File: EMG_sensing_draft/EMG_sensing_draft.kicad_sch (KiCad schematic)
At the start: 16 parts

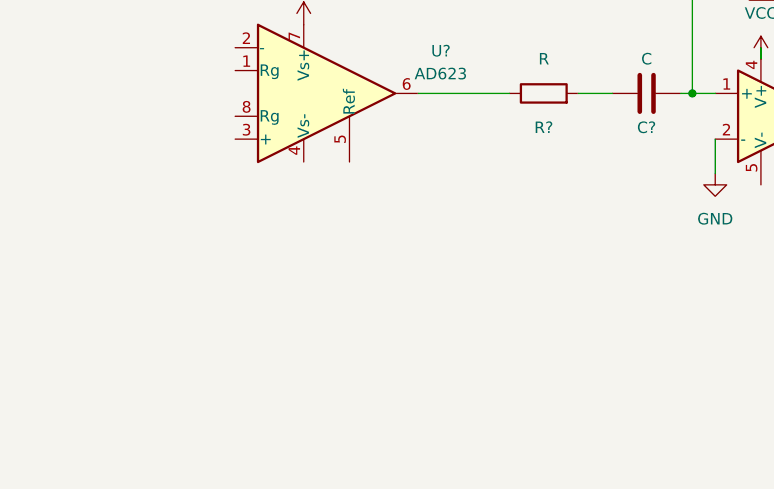
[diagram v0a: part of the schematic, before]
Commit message: Add parts folder and components
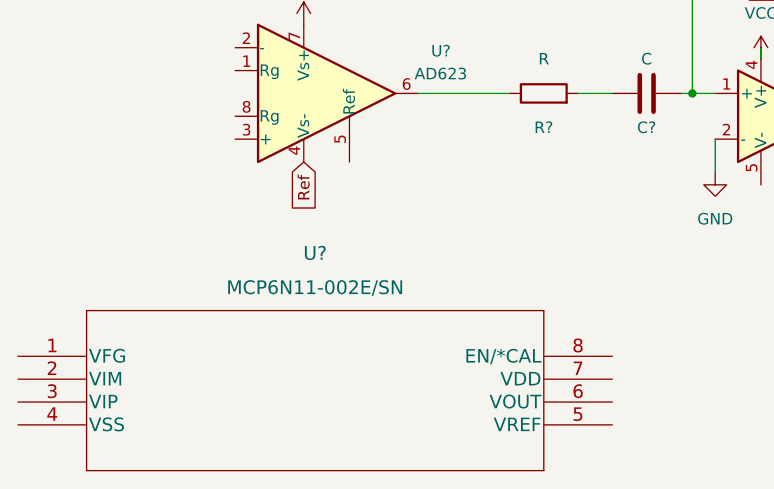
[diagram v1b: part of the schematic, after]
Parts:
- added U?: MCP6N11-002E/SN, SOIC8-N_MC_MCH, symbol MCP6N11:MCP6N11-002E/SN
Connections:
- net Ref: now reaches U?.4 (Vs-)
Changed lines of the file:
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@@
     (stroke (width 0) (type default) (color 0 0 0 0))
+  )
+  (global_label "Ref" (shape input) (at 66.04 109.22 270) (fields_autoplaced)
+    (effects (font (size 1.27 1.27)) (justify right))
+    (property "Intersheet References" "${INTERSHEET_REFS}" (id 0) (at 66.1194 114.7174 90)
+      (effects (font (size 1.27 1.27)) (justify right) hide)
+    )
   )
   (symbol (lib_id "Device:C") (at 229.87 85.09 90) (unit 1)
@@
     (pin "2")
   )
+  (symbol (lib_id "MCP6N11:MCP6N11-002E{slash}SN") (at 34.29 130.81 0) (unit 1)
+    (in_bom yes) (on_board yes) (fields_autoplaced)
+    (property "Reference" "U?" (id 0) (at 67.31 119.38 0)
+      (effects (font (size 1.524 1.524)))
+    )
+    (property "Value" "MCP6N11-002E/SN" (id 1) (at 67.31 123.19 0)
+      (effects (font (size 1.524 1.524)))
+    )
+    (property "Footprint" "SOIC8-N_MC_MCH" (id 2) (at 67.31 124.714 0)
+      (effects (font (size 1.524 1.524)) hide)
+    )
+    (property "Datasheet" "" (id 3) (at 34.29 130.81 0)
+      (effects (font (size 1.524 1.524)))
+    )
+    (pin "1")
+    (pin "2")
+    (pin "3")
+    (pin "4")
+    (pin "5")
+    (pin "6")
+    (pin "7")
+    (pin "8")
+  )
   (symbol (lib_id "Device:R") (at 156.21 90.17 90) (unit 1)
     (in_bom yes) (on_board yes)
@@
       (reference "R?") (unit 1) (value "R") (footprint "")
     )
+    (path "/4d7dc583-653d-4195-93a0-299e440aba51"
+      (reference "U?") (unit 1) (value "MCP6N11-002E/SN") (footprint "SOIC8-N_MC_MCH")
+    )
     (path "/6050b63c-7b0b-43e0-927f-cccf7bc57ee0"

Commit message: added Eclectronics folder
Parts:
- added J?: USB_A_0480370001, symbol Eclectronics:USB_A_0480370001
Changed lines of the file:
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@@
     (pin "1")
+  )
+  (symbol (lib_id "Eclectronics:USB_A_0480370001") (at 36.83 73.66 0) (unit 1)
+    (in_bom yes) (on_board yes) (fields_autoplaced)
+    (property "Reference" "J?" (id 0) (at 36.83 54.61 0)
+      (effects (font (size 1.524 1.524)))
+    )
+    (property "Value" "USB_A_0480370001" (id 1) (at 36.83 58.42 0)
+      (effects (font (size 1.524 1.524)))
+    )
+    (property "Footprint" "" (id 2) (at 45.72 69.85 0)
+      (effects (font (size 1.27 1.27)) hide)
+    )
+    (property "Datasheet" "" (id 3) (at 45.72 69.85 0)
+      (effects (font (size 1.27 1.27)) hide)
+    )
+    (pin "1")
+    (pin "2")
+    (pin "3")
+    (pin "4")
+    (pin "5")
+    (pin "6")
   )
   (symbol (lib_id "power:GND") (at 111.76 110.49 0) (unit 1)
@@
       (reference "D?") (unit 1) (value "DIODE") (footprint "")
     )
+    (path "/62cb1867-8881-4d82-894a-982d3e0ef0cf"
+      (reference "J?") (unit 1) (value "USB_A_0480370001") (footprint "")
+    )
     (path "/46275dcf-c1cf-4eed-86f4-1f3b88e55538"

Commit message: added inamp
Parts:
- removed U?: MCP6N11-002E/SN, SOIC8-N_MC_MCH, symbol MCP6N11:MCP6N11-002E/SN
- removed U?: AD623, symbol Amplifier_Instrumentation:AD623
- added J?: Conn_01x03, symbol Connector_Generic:Conn_01x03
- added R? (x2): R, symbol Device:R
- added U?: MCP6N11-002E/SN, SOIC8-N_MC_MCH, symbol MCP6N11:MCP6N11-002E/SN
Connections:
- net GND: now also U?.4 (VSS)
- net V_SIGNAL: now reaches C?.2, R?.2, U?.3
- net 5V: now reaches J?.1 (VBUS)
- net 5V: now also U?.7 (VDD)
- new net: R?.1, R?.2, U?.1 (VFG)
- new net VOUT: R?.2, U?.6 (VOUT)
- new net emg_node_one: J?.2 (Pin_2)
- new net emg_node_two: J?.1 (Pin_1)
- new net emg_ref: J?.3 (Pin_3), R?.1, U?.5 (VREF)
- new net emg_sensor_one: U?.2 (VIM)
- new net emg_sensor_two: U?.3 (VIP)
- no-connect marks 0 -> 3
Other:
- moved on the sheet: C?, D?, J?, R?, U?

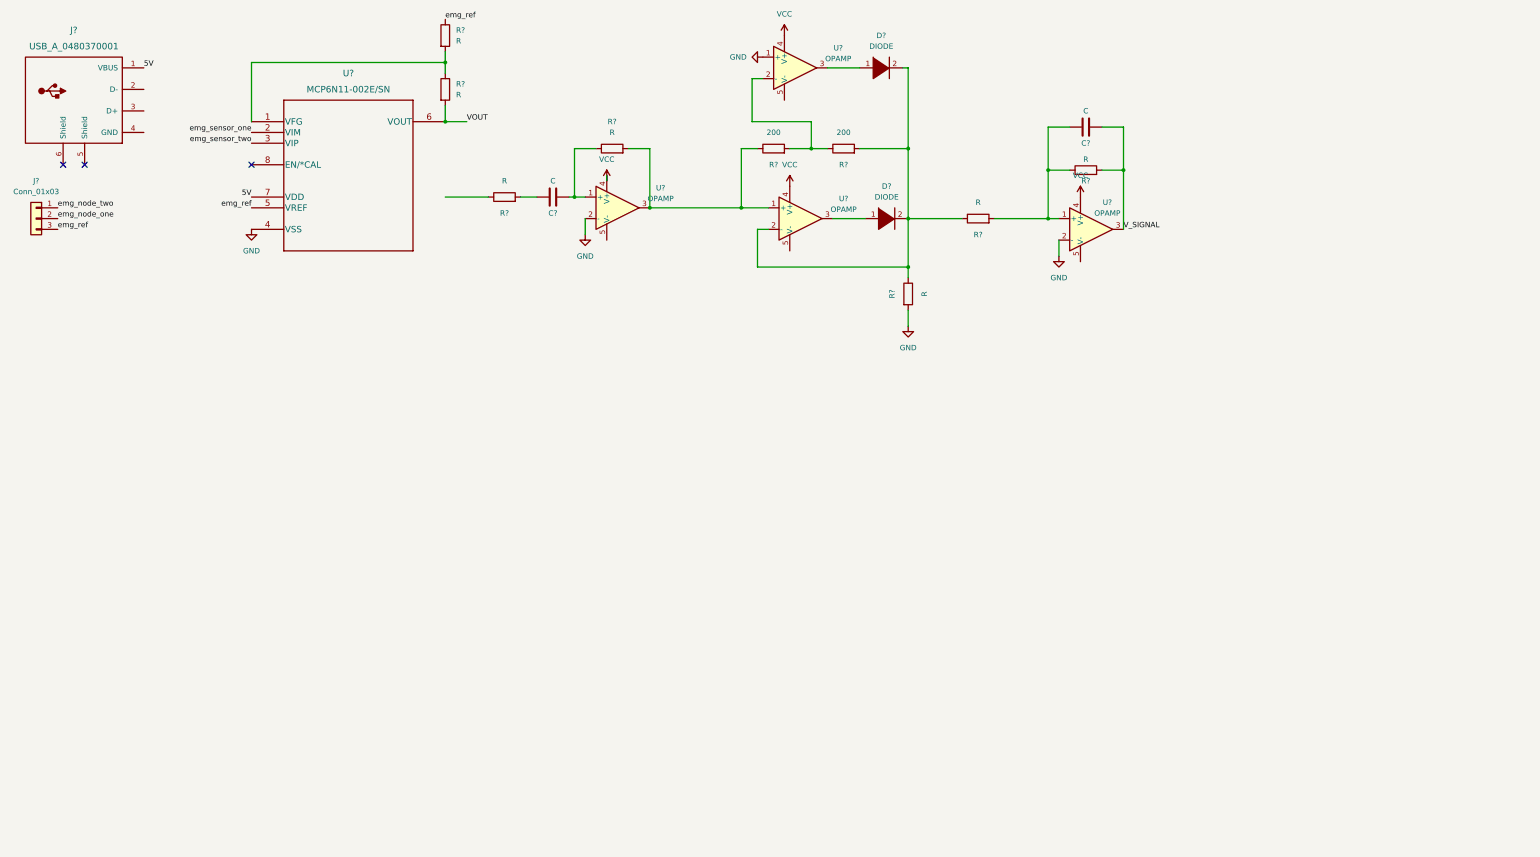
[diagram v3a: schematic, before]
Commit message: Add rp2040 to schematics
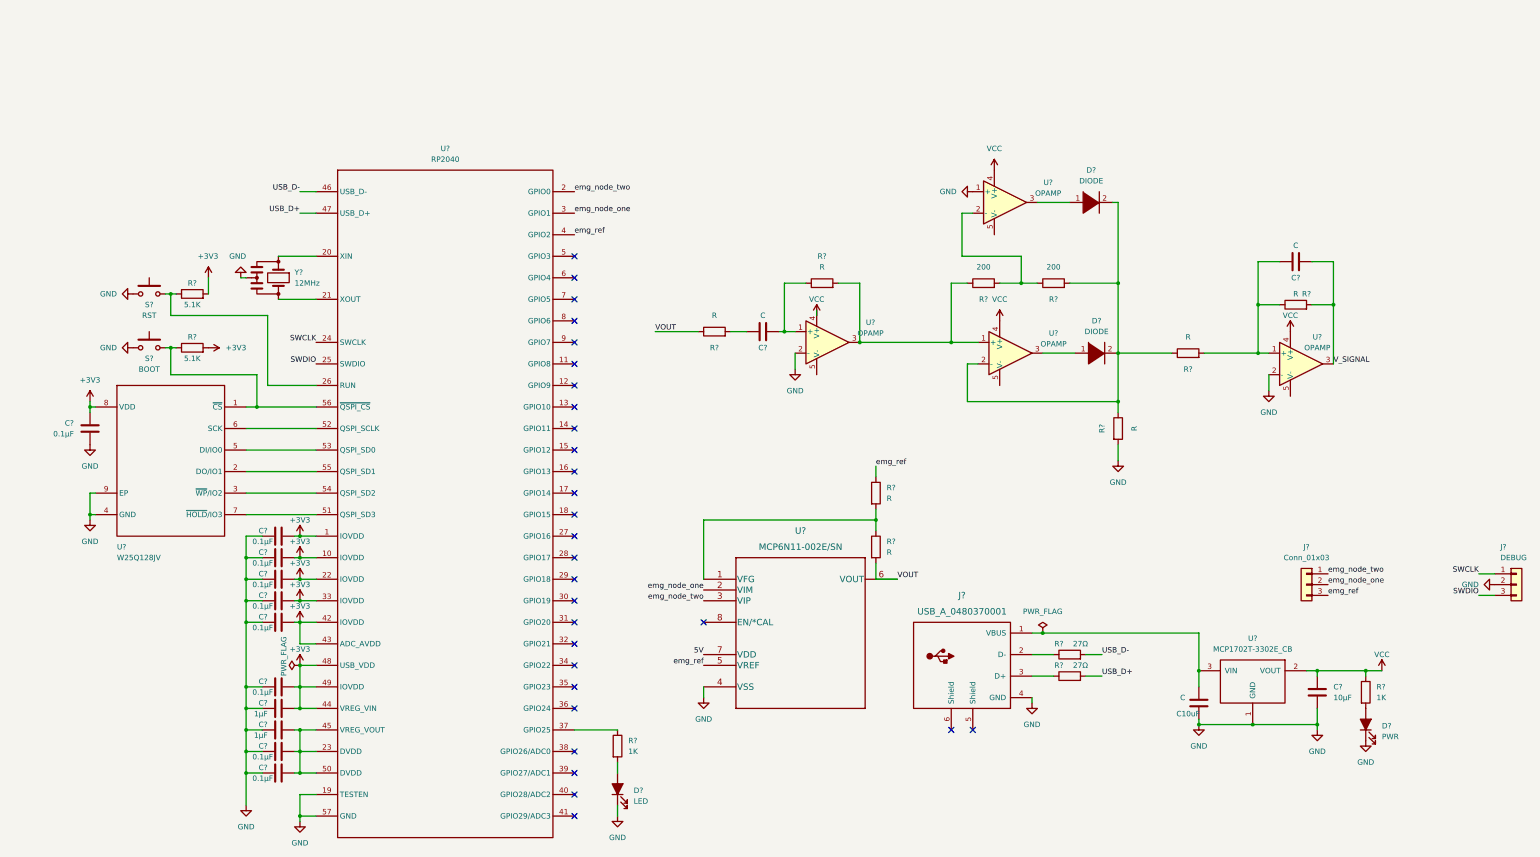
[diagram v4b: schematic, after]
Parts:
- added C10uF: C, symbol Device:C
- added C? (x2): 1µF, Capacitor_SMD:C_0402_1005Metric, symbol Device:C
- added C? (x8): 0.1µF, Capacitor_SMD:C_0402_1005Metric, symbol Device:C
- added C?: 10µF, Capacitor_SMD:C_0603_1608Metric, symbol Device:C
- added C?: 0.1µF, Resistor_SMD:R_0402_1005Metric, symbol Device:C
- added D?: LED, LED_SMD:LED_0805_2012Metric, symbol Device:LED_Filled
- added D?: PWR, LED_SMD:LED_0805_2012Metric, symbol Device:LED_Filled
- added J?: DEBUG, Connector_PinHeader_2.54mm:PinHeader_1x03_P2.54mm_Vertical, symbol Connector_Generic:Conn_01x03
- added R? (x2): 1K, Resistor_SMD:R_0402_1005Metric, symbol Device:R
- added R? (x2): 5.1K, Resistor_SMD:R_0402_1005Metric, symbol Device:R
- added R? (x2): 27Ω, Resistor_SMD:R_0402_1005Metric, symbol Device:R
- added S?: BOOT, Eclectronics:TL3301AFxxxxJ, symbol Eclectronics:SW
- added S?: RST, Eclectronics:TL3301AFxxxxJ, symbol Eclectronics:SW
- added U?: RP2040, symbol Eclectronics:RP2040
- added U?: MCP1702T-3302E_CB, symbol Eclectronics:MCP1702T-3302E_CB
- added U?: W25Q128JV, Package_SON:WSON-8-1EP_6x5mm_P1.27mm_EP3.4x4.3mm, symbol Eclectronics:W25Q128JV
- added Y?: 12MHz, Eclectronics:CSTNE, symbol Eclectronics:Crystal
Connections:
- net emg_sensor_one is gone; now on net emg_node_one: U?.2 (VIM)
- net emg_sensor_two is gone; now on net emg_node_two: U?.3 (VIP)
- net 5V: no longer J?.1 (VBUS)
- net GND: now also J?.4 (GND), C10uF.1, C?.1, C?.2, C?.2, C?.2, C?.2, C?.2, C?.2, C?.2, C?.2, C?.2, C?.2, C?.2, D?.1 (K), D?.1 (K), J?.2 (Pin_2), S?.1, S?.1, U?.1 (GND), U?.19 (TESTEN), U?.4 (GND), U?.57 (GND), U?.9 (EP), Y?.2
- net VCC: now also C?.1, R?.1, U?.2 (VOUT)
- net VOUT: now also R?.1
- net emg_node_one: now also U?.3 (GPIO1)
- net emg_node_two: now also U?.2 (GPIO0)
- net emg_ref: now also U?.4 (GPIO2)
- net at J?.2 (D-): now also R?.1
- net at J?.3 (D+): now also R?.1
- new net: R?.1, S?.2, U?.1 (~{CS}), U?.56 (~{QSPI_CS})
- new net: U?.20 (XIN), Y?.1
- new net: U?.21 (XOUT), Y?.3
- new net: C?.1, C?.1, C?.1, U?.23 (DVDD), U?.45 (VREG_VOUT), U?.50 (DVDD)
- new net: R?.1, S?.2, U?.26 (RUN)
- new net: R?.1, U?.37 (GPIO25)
- new net: U?.51 (QSPI_SD3), U?.7 (~{HOLD}/IO3)
- new net: U?.52 (QSPI_SCLK), U?.6 (SCK)
- new net: U?.5 (DI/IO0), U?.53 (QSPI_SD0)
- new net: U?.3 (~{WP}/IO2), U?.54 (QSPI_SD2)
- new net: U?.2 (DO/IO1), U?.55 (QSPI_SD1)
- new net: D?.2 (A), R?.2 (x2)
- new net: C10uF.2, J?.1 (VBUS), U?.3 (VIN)
- new net +3V3: C?.1, C?.1, C?.1, C?.1, C?.1, C?.1, C?.1, C?.2, R?.2, R?.2, U?.1 (IOVDD), U?.10 (IOVDD), U?.22 (IOVDD), U?.33 (IOVDD), U?.42 (IOVDD), U?.43 (ADC_AVDD), U?.44 (VREG_VIN), U?.48 (USB_VDD), U?.49 (IOVDD), U?.8 (VDD)
- new net SWCLK: J?.1 (Pin_1), U?.24 (SWCLK)
- new net SWDIO: J?.3 (Pin_3), U?.25 (SWDIO)
- new net USB_D+: R?.2, U?.47 (USB_D+)
- new net USB_D-: R?.2, U?.46 (USB_D-)
- no-connect marks 3 -> 29
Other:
- moved on the sheet: C?, D?, J?, R?, U?

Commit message: added BLE module and cleaned up schematic
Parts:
- removed R? (x2): 27Ω, Resistor_SMD:R_0402_1005Metric, symbol Device:R
- added D1: LED, symbol Device:LED
- added R3, R4: 27, symbol Device:R
- added R5: 1k, symbol Device:R
- added R7, R8, R9: R, symbol Device:R
- added U2: RN4871-I/RM140, RN4871_MCH, symbol RN4871:RN4871-I/RM140
- C13: renamed from C10uF; value C -> 10uF
- J1: renamed from J?; value Conn_01x03 -> EMG_SIGNAL
- gave numbers to parts that had none: 44
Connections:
- net 5V is gone; now on net +3V3: U8.7 (VDD)
- net VCC is gone; now on net +3V3: C14.1, R13.1, U4.4 (V+), U5.2 (VOUT), U6.4 (V+), U7.4 (V+), U9.4 (V+)
- net +3V3: now also D1.2 (A), U2.14 (VBAT)
- net GND: now also U4.5 (V-), U6.5 (V-), U7.5 (V-), U9.5 (V-), U2.13 (GND), U2.2 (GND)
- net USB_D+: now also J2.3 (D+), R4.2; no longer U3.47 (USB_D+)
- net USB_D-: now also J2.2 (D-), R3.1; no longer U3.46 (USB_D-)
- net V_SIGNAL: now also U3.41 (GPIO29/ADC3)
- net emg_node_one: now also R8.2; no longer J1.2 (Pin_2), U3.3 (GPIO1)
- net emg_node_two: now also R7.2; no longer J1.1 (Pin_1), U3.2 (GPIO0)
- net emg_ref: now also R9.2; no longer J1.3 (Pin_3), U3.4 (GPIO2)
- net CTS: now reaches U3.38 (GPIO26/ADC0)
- net CTS: now also U2.11 (P0_0)
- net RTS: now reaches U3.39 (GPIO27/ADC1)
- net RTS: now also U2.9 (P3_6)
- net RST_N: now reaches U3.40 (GPIO28/ADC2)
- net RST_N: now also U2.10 (RST_N)
- net at R19.2, U8.1 (VFG): now also R18.2; no longer R18.1
- net VOUT renamed V_DIFF
- net V_DIFF: now also R18.1; no longer R18.2
- new net: R3.2, U3.46 (USB_D-)
- new net: R4.1, U3.47 (USB_D+)
- new net: J1.1 (Pin_1), R7.1
- new net: R5.1, U2.12 (P0_2)
- new net: D1.1 (K), R5.2
- new net: J1.2 (Pin_2), R8.1
- new net: J1.3 (Pin_3), R9.1
- new net BLE_RX: U2.7 (UART_RX), U3.2 (GPIO0)
- new net BLE_TX: U2.8 (UART_TX), U3.3 (GPIO1)
- new net RX_IND: U2.6 (P1_6), U3.4 (GPIO2)
- no-connect marks 29 -> 30
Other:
- note added: "BANDPASS FILTER AND RECTIFICATION"
- note added: "BLE MODULE"
- note added: "DIFFERENTIAL AMPLIFIER"
- note added: "PIN HEADERS"
- note added: "POWER SOURCE"
- note added: "RP2040 + MEMORY UNIT"
- moved on the sheet: C1, C10, C11, C12, C13, C14, C15, C2, C3, C4, C5, C6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

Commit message: Add R and C values (please check!)
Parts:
- C12: value C -> 100uF
- C15: value C -> 1uF
- R10: value R -> 75
- R11: value R -> 750
- R15: value R -> 499
- R16: value R -> 316
- R17: value R -> 909
- R18: value R -> 200k
- R19: value R -> 10k
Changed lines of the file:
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@@
     (in_bom yes) (on_board yes)
     (property "Reference" "C15" (id 0) (at 314.96 110.49 90))
-    (property "Value" "C" (id 1) (at 314.96 102.87 90))
+    (property "Value" "1uF" (id 1) (at 314.96 102.87 90))
     (property "Footprint" "" (id 2) (at 318.77 105.7148 0)
       (effects (font (size 1.27 1.27)) hide)
@@
     (in_bom yes) (on_board yes)
     (property "Reference" "C12" (id 0) (at 189.23 127 90))
-    (property "Value" "C" (id 1) (at 189.23 119.38 90))
+    (property "Value" "100uF" (id 1) (at 189.23 119.38 90))
     (property "Footprint" "" (id 2) (at 193.04 122.2248 0)
       (effects (font (size 1.27 1.27)) hide)
@@
   (symbol (lib_id "Device:R") (at 314.96 116.84 90) (unit 1)
     (in_bom yes) (on_board yes)
-    (property "Reference" "R17" (id 0) (at 317.5 114.3 90))
-    (property "Value" "R" (id 1) (at 314.96 114.3 90))
+    (property "Reference" "R17" (id 0) (at 314.96 119.38 90))
+    (property "Value" "909" (id 1) (at 314.96 114.3 90))
     (property "Footprint" "" (id 2) (at 314.96 118.618 90)
       (effects (font (size 1.27 1.27)) hide)
@@
     (in_bom yes) (on_board yes)
     (property "Reference" "R16" (id 0) (at 289.56 132.08 90))
-    (property "Value" "R" (id 1) (at 289.56 124.46 90))
+    (property "Value" "316" (id 1) (at 289.56 124.46 90))
     (property "Footprint" "" (id 2) (at 289.56 130.048 90)
       (effects (font (size 1.27 1.27)) hide)
@@
     (in_bom yes) (on_board yes)
     (property "Reference" "R15" (id 0) (at 269.24 146.05 90))
-    (property "Value" "R" (id 1) (at 276.86 146.05 90))
+    (property "Value" "499" (id 1) (at 276.86 146.05 90))
     (property "Footprint" "" (id 2) (at 271.272 146.05 90)
       (effects (font (size 1.27 1.27)) hide)
@@
       (effects (font (size 1.27 1.27)) hide)
     )
-    (property "Value" "+3V3" (id 1) (at 313.69 119.38 0))
+    (property "Value" "+3V3" (id 1) (at 317.5 121.92 0))
     (property "Footprint" "" (id 2) (at 313.69 123.19 0)
       (effects (font (size 1.27 1.27)) hide)
@@
     (in_bom yes) (on_board yes) (fields_autoplaced)
     (property "Reference" "R11" (id 0) (at 203.2 105.41 90))
-    (property "Value" "R" (id 1) (at 203.2 107.95 90))
+    (property "Value" "750" (id 1) (at 203.2 107.95 90))
     (property "Footprint" "" (id 2) (at 203.2 113.538 90)
       (effects (font (size 1.27 1.27)) hide)
@@
     (in_bom yes) (on_board yes) (fields_autoplaced)
     (property "Reference" "R19" (id 0) (at 334.01 21.59 90))
-    (property "Value" "R" (id 1) (at 334.01 24.13 90))
+    (property "Value" "10k" (id 1) (at 334.01 24.13 90))
     (property "Footprint" "" (id 2) (at 334.01 26.162 90)
       (effects (font (size 1.27 1.27)) hide)
@@
     (in_bom yes) (on_board yes)
     (property "Reference" "R10" (id 0) (at 177.8 127 90))
-    (property "Value" "R" (id 1) (at 177.8 119.38 90))
+    (property "Value" "75" (id 1) (at 177.8 119.38 90))
     (property "Footprint" "" (id 2) (at 177.8 124.968 90)
       (effects (font (size 1.27 1.27)) hide)
@@
     (in_bom yes) (on_board yes) (fields_autoplaced)
     (property "Reference" "R18" (id 0) (at 323.85 21.59 90))
-    (property "Value" "R" (id 1) (at 323.85 24.13 90))
+    (property "Value" "200k" (id 1) (at 323.85 24.13 90))
     (property "Footprint" "" (id 2) (at 323.85 29.718 90)
       (effects (font (size 1.27 1.27)) hide)
@@
     )
     (path "/43e01833-ec1e-4b59-bb68-ae08e8b6ad87"
-      (reference "C12") (unit 1) (value "C") (footprint "")
+      (reference "C12") (unit 1) (value "100uF") (footprint "")
     )
     (path "/2d833c17-71e7-42c7-b9f3-0c31cf2e96e2"
@@
     )
     (path "/0392a271-4134-41ca-8350-e6e1460a370e"
-      (reference "C15") (unit 1) (value "C") (footprint "")
+      (reference "C15") (unit 1) (value "1uF") (footprint "")
     )
     (path "/edc6d0d1-95cd-4bd8-8476-e09b97bf0890"
@@
     )
     (path "/f5f70325-2f2b-4456-91b6-bfaa64c06ac6"
-      (reference "R10") (unit 1) (value "R") (footprint "")
+      (reference "R10") (unit 1) (value "75") (footprint "")
     )
     (path "/d46886d9-0779-4f34-b71d-ecc81f690686"
-      (reference "R11") (unit 1) (value "R") (footprint "")
+      (reference "R11") (unit 1) (value "750") (footprint "")
     )
     (path "/4dc60790-bc81-4a6a-8037-22403ba4bbd0"
@@
     )
     (path "/972e1a76-c2d1-4126-8f32-c7cf83e48735"
-      (reference "R15") (unit 1) (value "R") (footprint "")
+      (reference "R15") (unit 1) (value "499") (footprint "")
     )
     (path "/945e681d-6586-4d02-be7d-fabbb657f6d9"
-      (reference "R16") (unit 1) (value "R") (footprint "")
+      (reference "R16") (unit 1) (value "316") (footprint "")
     )
     (path "/4d287f70-ea46-43ca-bdf4-5c6ce3fdd17a"
-      (reference "R17") (unit 1) (value "R") (footprint "")
+      (reference "R17") (unit 1) (value "909") (footprint "")
     )
     (path "/fa5c19a9-e166-4278-a194-10b490cea57b"
-      (reference "R18") (unit 1) (value "R") (footprint "")
+      (reference "R18") (unit 1) (value "200k") (footprint "")
     )
     (path "/da79afc4-af21-4b93-aaed-4ca701f6b222"
-      (reference "R19") (unit 1) (value "R") (footprint "")
+      (reference "R19") (unit 1) (value "10k") (footprint "")
     )
     (path "/d1933b1f-6869-42d3-b087-953b55088154"

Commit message: updated RC filter characteristic freq
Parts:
- C15: value 1uF -> 0.33uF
- D2: value LED -> TEST
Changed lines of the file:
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@@
     (in_bom yes) (on_board yes)
     (property "Reference" "C15" (id 0) (at 314.96 110.49 90))
-    (property "Value" "1uF" (id 1) (at 314.96 102.87 90))
+    (property "Value" "0.33uF" (id 1) (at 314.96 102.87 90))
     (property "Footprint" "" (id 2) (at 318.77 105.7148 0)
       (effects (font (size 1.27 1.27)) hide)
@@
       (effects (font (size 1.27 1.27)) (justify right))
     )
-    (property "Value" "LED" (id 1) (at 151.13 173.0374 90)
+    (property "Value" "TEST" (id 1) (at 151.13 173.0374 90)
       (effects (font (size 1.27 1.27)) (justify right))
     )
@@
     )
     (path "/0392a271-4134-41ca-8350-e6e1460a370e"
-      (reference "C15") (unit 1) (value "1uF") (footprint "")
+      (reference "C15") (unit 1) (value "0.33uF") (footprint "")
     )
     (path "/edc6d0d1-95cd-4bd8-8476-e09b97bf0890"
@@
     )
     (path "/2a4820de-c377-4e03-8775-f5a166966ff3"
-      (reference "D2") (unit 1) (value "LED") (footprint "LED_SMD:LED_0805_2012Metric")
+      (reference "D2") (unit 1) (value "TEST") (footprint "LED_SMD:LED_0805_2012Metric")
     )
     (path "/b2ef5382-c93c-433d-bae6-7949c1a7f81b"
